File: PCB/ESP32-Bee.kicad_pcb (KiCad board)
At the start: 2 copper layers, 26 x 29 mm, 33 parts, among them J1 M22-2511005, J2 M22-2511005, SW1 B3U-1000P, T1 1909763-1, U1 ESP32, U2 W25Q64FWSSIG, X1 FA-128_26.0000MF10Z-AC3

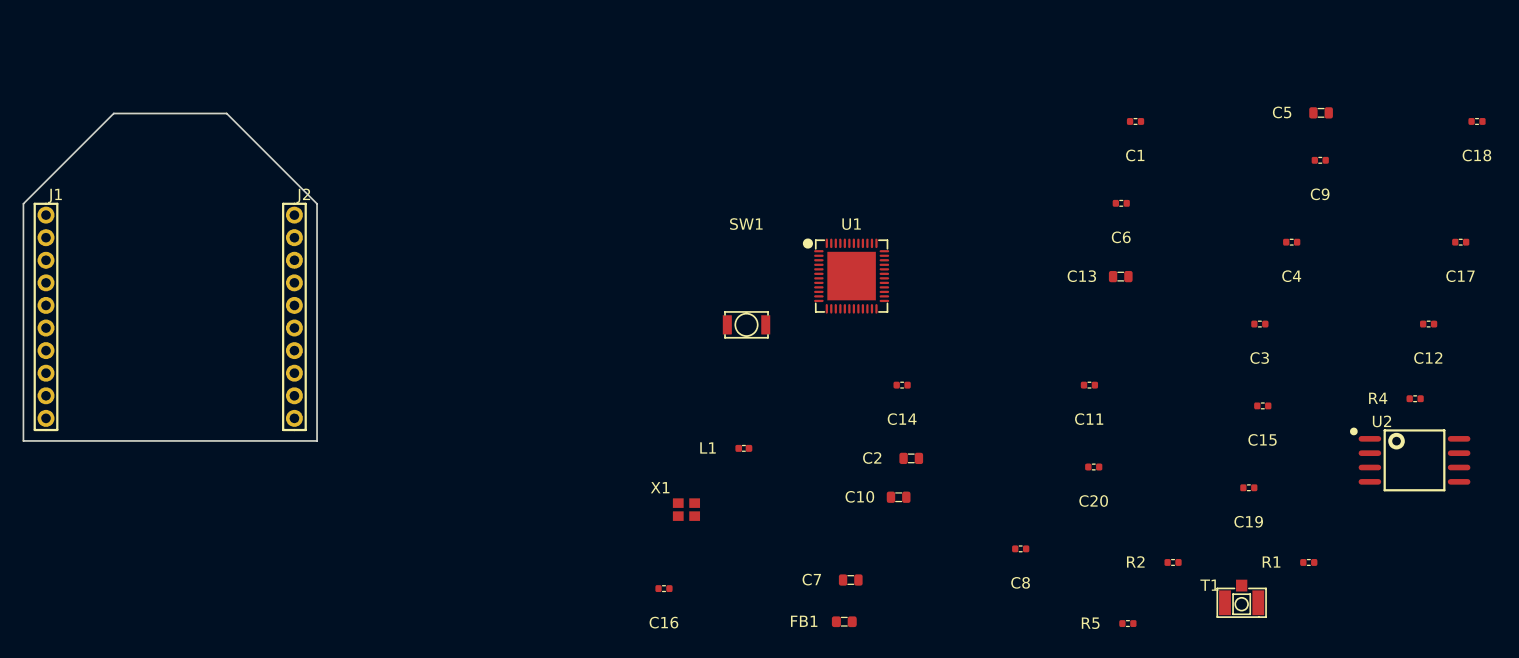
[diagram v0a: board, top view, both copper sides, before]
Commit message: More Progress
More progress with the PCB, having a hard time finding a RF shielf that
is XBee pro sized.
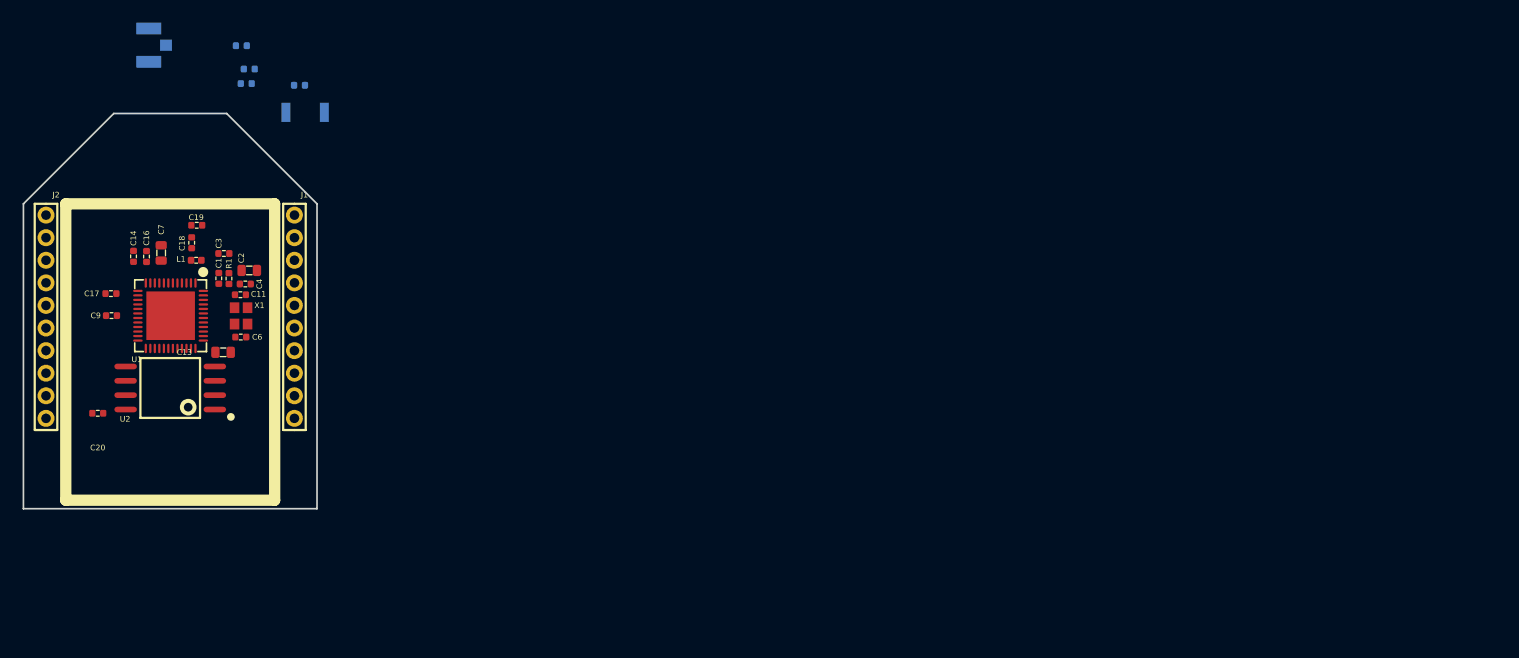
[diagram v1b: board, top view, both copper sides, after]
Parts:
- removed C10, C5: CL10A106KQ8NNNC, PCB_Footprints:C0603
- removed C12: CL05A105KA5NQNC, PCB_Footprints:C0402
- removed C15: CL05B104JP5NNNC, PCB_Footprints:C0402
- removed FB1: MI0603K300R-10, PCB_Footprints:MI0603K300R-10
- C8, R2, R4, R5, SW1, T1: moved to B.Cu
- moved C17 119.6 mm to (115.8, 58.0), turned to 180 degrees
- moved C18 114.3 mm to (122.9, 53.5), turned to 90 degrees
- moved U2 110.4 mm to (121.0, 66.3), turned to 180 degrees
- moved T1 108.7 mm to (119.1, 36.0), turned to 90 degrees
- moved R4 108.5 mm to (127.3, 36.0)
- moved C9 107.9 mm to (115.8, 59.9), turned to 180 degrees
- moved R1 98.9 mm to (126.2, 56.6), turned to 90 degrees
- moved C19 96.0 mm to (123.3, 51.9)
- moved C4 92.7 mm to (127.7, 57.1)
- moved R2 92.4 mm to (127.7, 39.4)
- moved R5 92.0 mm to (128.0, 38.1)
- moved C3 92.0 mm to (125.8, 54.4)
- moved C20 88.3 mm to (114.6, 68.5)
- moved C1 82.4 mm to (125.3, 56.6), turned to 90 degrees
- moved C13 79.8 mm to (125.7, 63.1)
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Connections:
- J1 pad 1: /PWR_IN -> +3V3
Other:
- board size 26 x 29 mm -> 26 x 35 mm
- net class Default: clearance 0.2 -> 0.1524; trace_width 0.25 -> 0.1524; via_dia 0.8 -> 0.635; via_drill 0.4 -> 0.3302
- rule trace_clearance: 0.2 -> 0.1524
- rule trace_min: 0.2 -> 0.1524
- rule via_min_drill: 0.3 -> 0.3302
- rule via_min_size: 0.4 -> 0.635
